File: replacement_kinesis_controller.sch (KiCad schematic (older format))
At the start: 23 parts

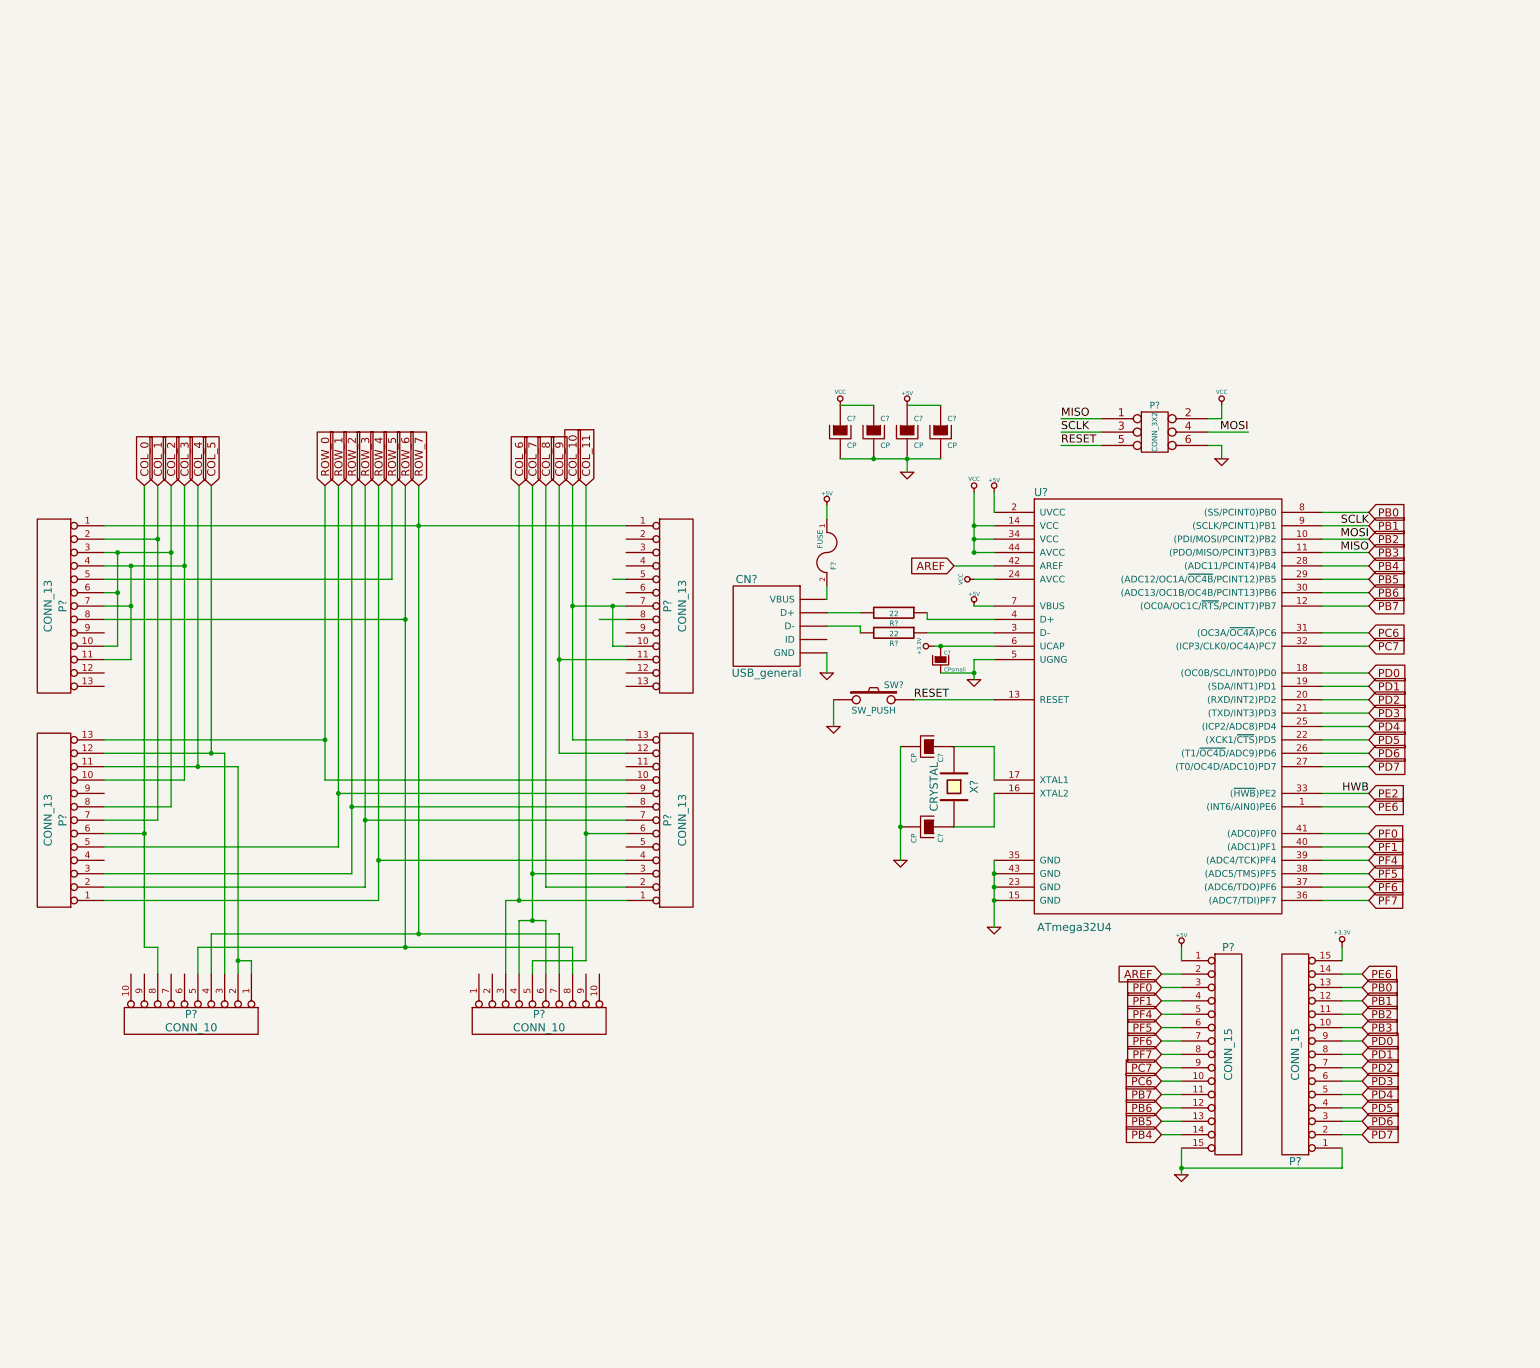
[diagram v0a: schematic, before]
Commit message: Updated schematic with matrix info
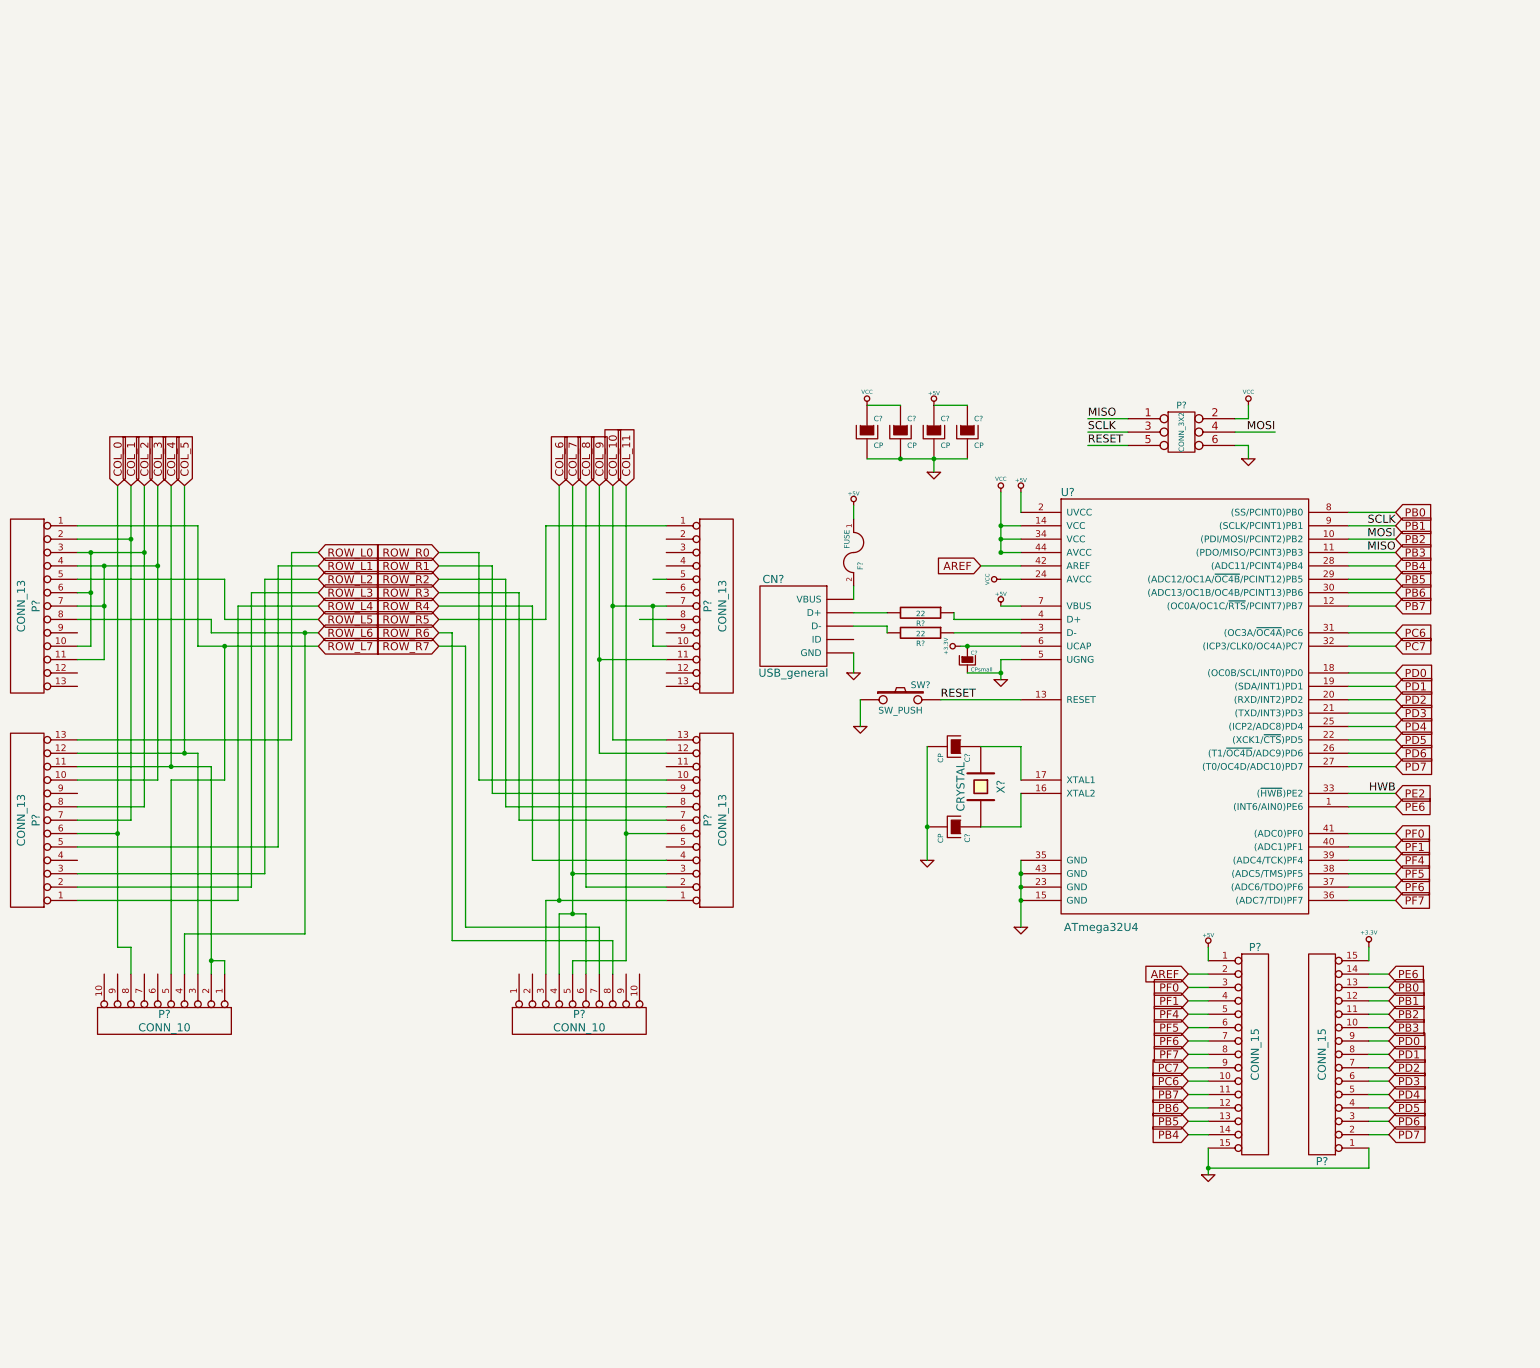
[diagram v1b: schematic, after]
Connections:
- net ROW_0 renamed ROW_L0
- net ROW_L0: no longer P?.10 (P10)
- net ROW_1 renamed ROW_L1
- net ROW_L1: no longer P?.9 (P9)
- net ROW_2 renamed ROW_L2
- net ROW_L2: no longer P?.8 (P8)
- net ROW_3 renamed ROW_L3
- net ROW_L3: no longer P?.7 (P7)
- net ROW_4 renamed ROW_L4
- net ROW_L4: no longer P?.4 (P4)
- net ROW_5 renamed ROW_L5
- removed net ROW_6: P?.5 (P5), P?.8 (P8), P?.8 (P8)
- removed net ROW_7: P?.1 (P1), P?.1 (P1), P?.4 (P4), P?.7 (P7)
- new net ROW_L6: P?.4 (P4), P?.8 (P8)
- new net ROW_L7: P?.1 (P1), P?.5 (P5)
- new net ROW_R0: P?.10 (P10)
- new net ROW_R1: P?.9 (P9)
- new net ROW_R2: P?.8 (P8)
- new net ROW_R3: P?.7 (P7)
- new net ROW_R4: P?.4 (P4)
- new net ROW_R5: P?.1 (P1)
- new net ROW_R6: P?.8 (P8)
- new net ROW_R7: P?.7 (P7)
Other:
- moved on the sheet: C?, CN?, F?, P?, R?, SW?, U?, X?

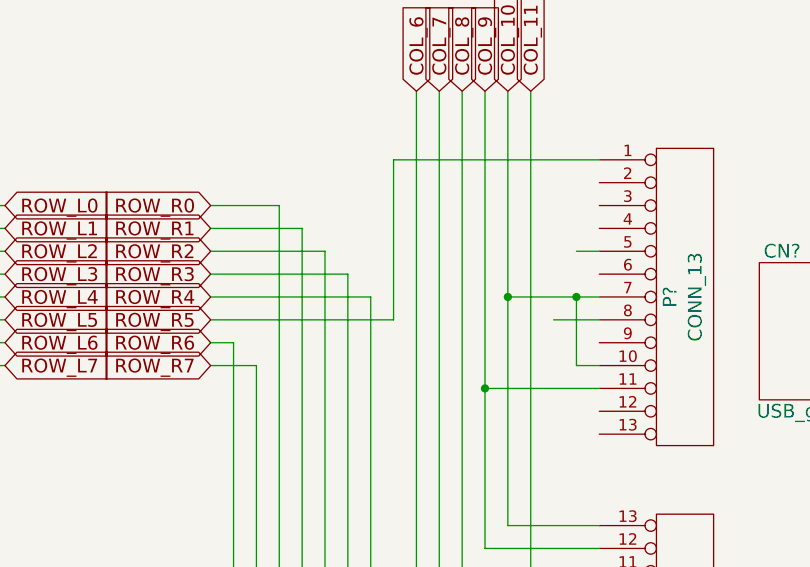
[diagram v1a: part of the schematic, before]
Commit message: Fix up right function key matrix
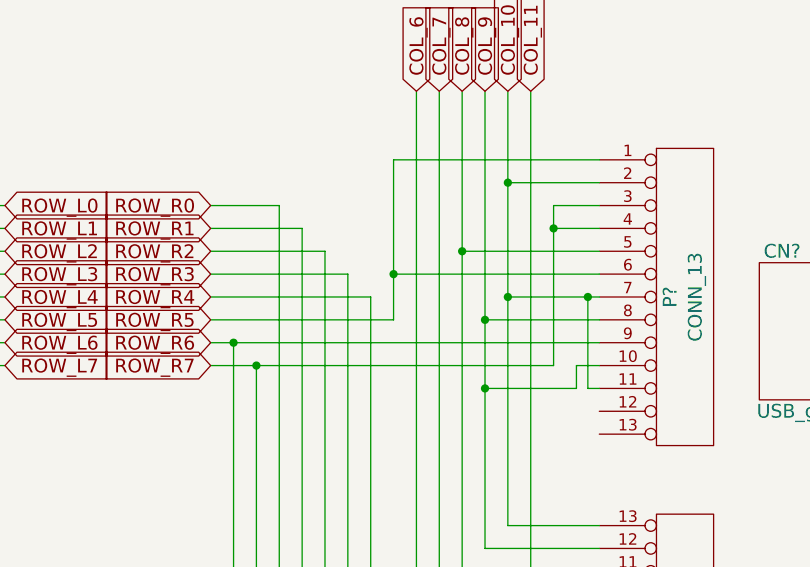
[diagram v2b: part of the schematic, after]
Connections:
- net COL_10: now also P?.11 (P11), P?.2 (P2); no longer P?.10 (P10)
- net COL_8: now also P?.5 (P5)
- net COL_9: now also P?.10 (P10), P?.8 (P8); no longer P?.11 (P11)
- net ROW_R5: now also P?.6 (P6)
- net ROW_R6: now also P?.9 (P9)
- net ROW_R7: now also P?.3 (P3), P?.4 (P4)
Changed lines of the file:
@@
 Connection ~ 1200 2200
 Wire Wire Line
-	5400 2000 5300 2000
-Wire Wire Line
 	5400 2200 5000 2200
 Wire Wire Line
 	5000 1300 5000 3200
-Wire Wire Line
-	5200 2300 5400 2300
-Wire Wire Line
-	5400 2500 5300 2500
-Wire Wire Line
-	5300 2500 5300 2200
-Connection ~ 5300 2200
-Wire Wire Line
-	5400 2600 4900 2600
 Wire Wire Line
 	4900 1300 4900 3300
@@
 	4000 1800 3700 1800
 Wire Wire Line
-	3700 2500 3900 2500
+	3700 2500 5200 2500
 Wire Wire Line
 	4700 1300 4700 4500
@@
 	3800 4700 3800 2400
 Wire Wire Line
-	3800 2400 3700 2400
+	3700 2400 5400 2400
+Wire Wire Line
+	5400 1700 5000 1700
+Connection ~ 5000 1700
+Wire Wire Line
+	5400 1800 5200 1800
+Wire Wire Line
+	5200 1800 5200 2500
+Connection ~ 3900 2500
+Wire Wire Line
+	5400 1900 5200 1900
+Connection ~ 5200 1900
+Wire Wire Line
+	5400 2000 4800 2000
+Connection ~ 4800 2000
+Wire Wire Line
+	5400 2100 4500 2100
+Connection ~ 4500 2100
+Wire Wire Line
+	5400 2300 4900 2300
+Connection ~ 4900 2300
+Connection ~ 3800 2400
+Wire Wire Line
+	5400 2500 5300 2500
+Wire Wire Line
+	5300 2500 5300 2600
+Wire Wire Line
+	5300 2600 4900 2600
+Wire Wire Line
+	5400 2600 5350 2600
+Wire Wire Line
+	5350 2600 5350 2200
+Connection ~ 5350 2200
 $EndSCHEMATC

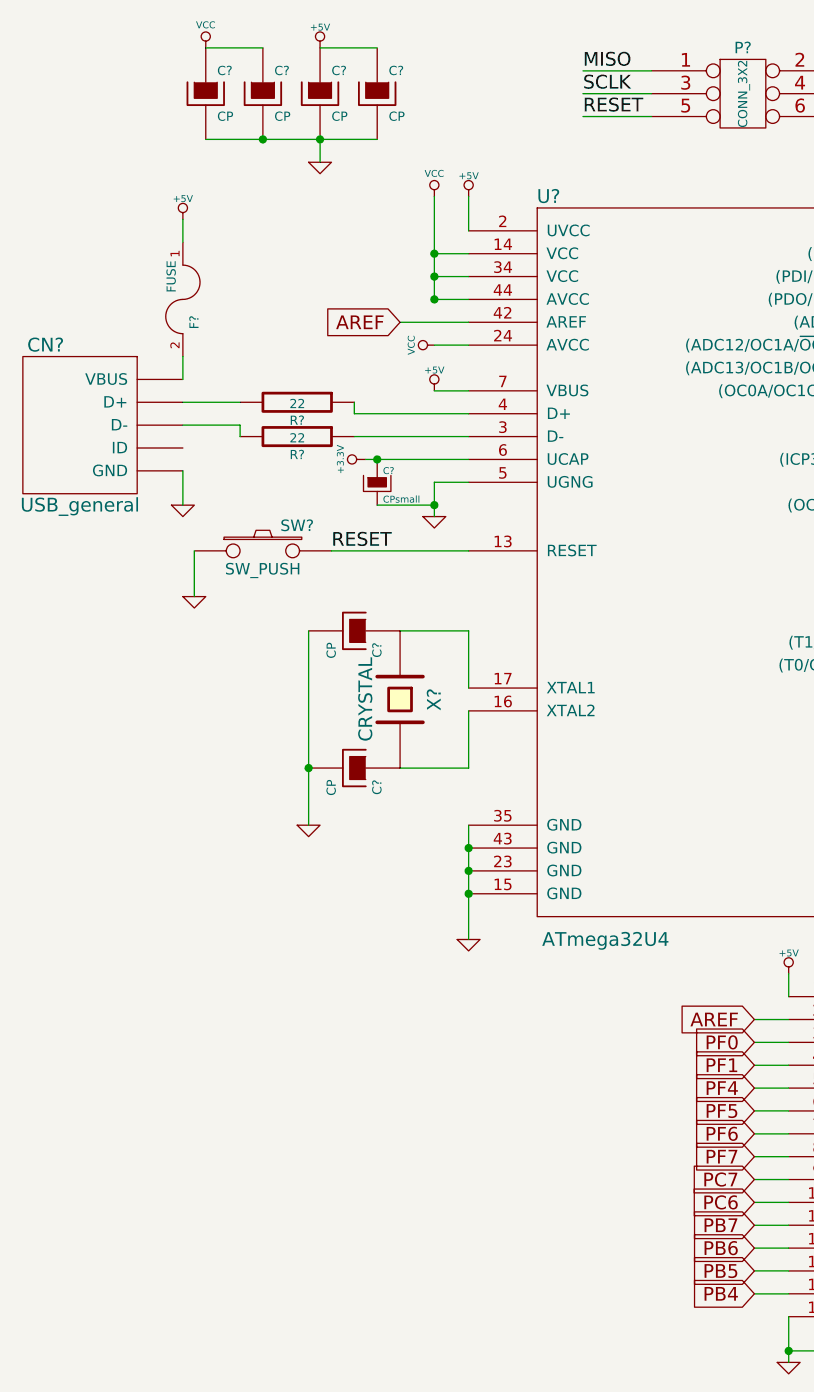
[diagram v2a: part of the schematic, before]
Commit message: Add value and extras for 32u4 breakout schematic
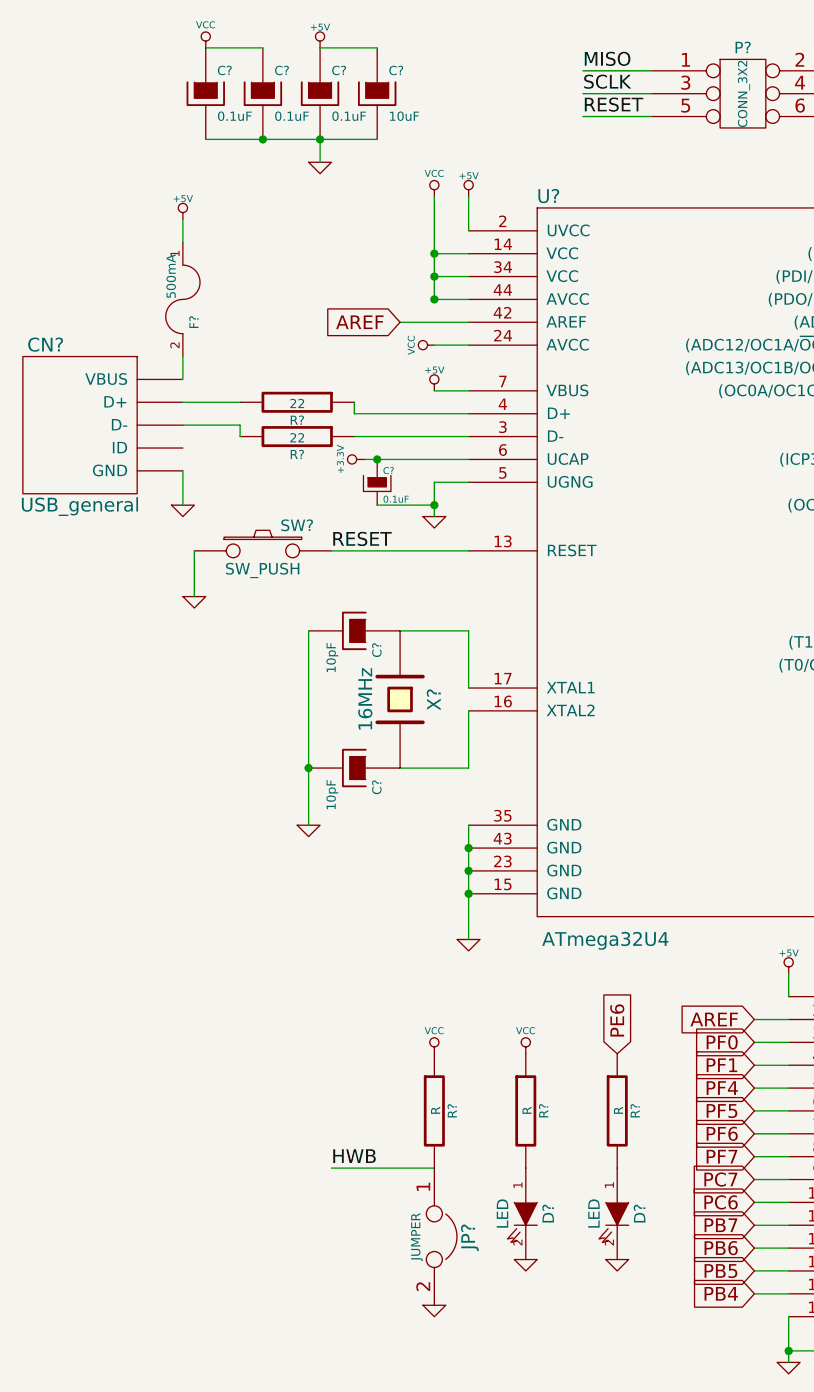
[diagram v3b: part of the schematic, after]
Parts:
- added D? (x2): LED, symbol LED
- added JP?: JUMPER, symbol JUMPER
- added R? (x3): R, symbol R
- C? (x2): value CP -> 10pF
- C?: value CPsmall -> 0.1uF
- C? (x3): value CP -> 0.1uF
- C?: value CP -> 10uF
- F?: value FUSE -> 500mA
- X?: value CRYSTAL -> 16MHz
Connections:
- net GND: now also D?.2 (K), D?.2 (K), JP?.2
- net PE2: now also JP?.1, R?.2
- net PE6: now also R?.1
- net VCC: now also R?.1, R?.1
- new net: D?.1 (A), R?.2 (x2)
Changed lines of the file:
@@
 P 7750 3550
 F 0 "X?" H 7750 3700 60  0000 C CNN
-F 1 "CRYSTAL" H 7750 3400 60  0000 C CNN
+F 1 "16MHz" H 7750 3400 60  0000 C CNN
 F 2 "" H 7750 3550 60  0000 C CNN
 F 3 "" H 7750 3550 60  0000 C CNN
@@
 P 7550 3850
 F 0 "C?" H 7600 3950 40  0000 L CNN
-F 1 "CP" H 7600 3750 40  0000 L CNN
+F 1 "10pF" H 7600 3750 40  0000 L CNN
 F 2 "" H 7650 3700 30  0000 C CNN
 F 3 "" H 7550 3850 300 0000 C CNN
@@
 P 7550 3250
 F 0 "C?" H 7600 3350 40  0000 L CNN
-F 1 "CP" H 7600 3150 40  0000 L CNN
+F 1 "10pF" H 7600 3150 40  0000 L CNN
 F 2 "" H 7650 3100 30  0000 C CNN
 F 3 "" H 7550 3250 300 0000 C CNN
@@
 P 6800 1800
 F 0 "F?" H 6900 1850 40  0000 C CNN
-F 1 "FUSE" H 6700 1750 40  0000 C CNN
+F 1 "500mA" H 6700 1750 40  0000 C CNN
 F 2 "" H 6800 1800 60  0000 C CNN
 F 3 "" H 6800 1800 60  0000 C CNN
@@
 P 7650 2600
 F 0 "C?" H 7675 2650 30  0000 L CNN
-F 1 "CPsmall" H 7675 2525 30  0000 L CNN
+F 1 "0.1uF" H 7675 2525 30  0000 L CNN
 F 2 "" H 7650 2600 60  0000 C CNN
 F 3 "" H 7650 2600 60  0000 C CNN
@@
 P 6900 900
 F 0 "C?" H 6950 1000 40  0000 L CNN
-F 1 "CP" H 6950 800 40  0000 L CNN
+F 1 "0.1uF" H 6950 800 40  0000 L CNN
 F 2 "" H 7000 750 30  0000 C CNN
 F 3 "" H 6900 900 300 0000 C CNN
@@
 P 7150 900
 F 0 "C?" H 7200 1000 40  0000 L CNN
-F 1 "CP" H 7200 800 40  0000 L CNN
+F 1 "0.1uF" H 7200 800 40  0000 L CNN
 F 2 "" H 7250 750 30  0000 C CNN
 F 3 "" H 7150 900 300 0000 C CNN
@@
 P 7400 900
 F 0 "C?" H 7450 1000 40  0000 L CNN
-F 1 "CP" H 7450 800 40  0000 L CNN
+F 1 "0.1uF" H 7450 800 40  0000 L CNN
 F 2 "" H 7500 750 30  0000 C CNN
 F 3 "" H 7400 900 300 0000 C CNN
@@
 P 7650 900
 F 0 "C?" H 7700 1000 40  0000 L CNN
-F 1 "CP" H 7700 800 40  0000 L CNN
+F 1 "10uF" H 7700 800 40  0000 L CNN
 F 2 "" H 7750 750 30  0000 C CNN
 F 3 "" H 7650 900 300 0000 C CNN
@@
 	5350 2600 5350 2200
 Connection ~ 5350 2200
+$Comp
+L R R?
+U 1 1 54C9D2DF
+P 7900 5350
+F 0 "R?" V 7980 5350 40  0000 C CNN
+F 1 "R" V 7907 5351 40  0000 C CNN
+F 2 "" V 7830 5350 30  0000 C CNN
+F 3 "" H 7900 5350 30  0000 C CNN
+	1    7900 5350
+	1    0    0    -1
+$EndComp
+$Comp
+L R R?
+U 1 1 54C9D340
+P 8700 5350
+F 0 "R?" V 8780 5350 40  0000 C CNN
+F 1 "R" V 8707 5351 40  0000 C CNN
+F 2 "" V 8630 5350 30  0000 C CNN
+F 3 "" H 8700 5350 30  0000 C CNN
+	1    8700 5350
+	1    0    0    -1
+$EndComp
+$Comp
+L R R?
+U 1 1 54C9D377
+P 8300 5350
+F 0 "R?" V 8380 5350 40  0000 C CNN
+F 1 "R" V 8307 5351 40  0000 C CNN
+F 2 "" V 8230 5350 30  0000 C CNN
+F 3 "" H 8300 5350 30  0000 C CNN
+	1    8300 5350
+	1    0    0    -1
+$EndComp
+$Comp
+L LED D?
+U 1 1 54C9D45A
+P 8300 5800
+F 0 "D?" H 8300 5900 50  0000 C CNN
+F 1 "LED" H 8300 5700 50  0000 C CNN
+F 2 "" H 8300 5800 60  0000 C CNN
+F 3 "" H 8300 5800 60  0000 C CNN
+	1    8300 5800
+	0    1    1    0
+$EndComp
+$Comp
+L LED D?
+U 1 1 54C9D4B9
+P 8700 5800
+F 0 "D?" H 8700 5900 50  0000 C CNN
+F 1 "LED" H 8700 5700 50  0000 C CNN
+F 2 "" H 8700 5800 60  0000 C CNN
+F 3 "" H 8700 5800 60  0000 C CNN
+	1    8700 5800
+	0    1    1    0
+$EndComp
+$Comp
+L JUMPER JP?
+U 1 1 54C9D61C
+P 7900 5900
+F 0 "JP?" H 7900 6050 60  0000 C CNN
+F 1 "JUMPER" H 7900 5820 40  0000 C CNN
+F 2 "" H 7900 5900 60  0000 C CNN
+F 3 "" H 7900 5900 60  0000 C CNN
+	1    7900 5900
+	0    1    1    0
+$EndComp
+$Comp
+L VCC #PWR?
+U 1 1 54C9D8DB
+P 8300 5100
+F 0 "#PWR?" H 8300 5200 30  0001 C CNN
+F 1 "VCC" H 8300 5200 30  0000 C CNN
+F 2 "" H 8300 5100 60  0000 C CNN
+F 3 "" H 8300 5100 60  0000 C CNN
+	1    8300 5100
+	1    0    0    -1
+$EndComp
+$Comp
+L VCC #PWR?
+U 1 1 54C9D977
+P 7900 5100
+F 0 "#PWR?" H 7900 5200 30  0001 C CNN
+F 1 "VCC" H 7900 5200 30  0000 C CNN
+F 2 "" H 7900 5100 60  0000 C CNN
+F 3 "" H 7900 5100 60  0000 C CNN
+	1    7900 5100
+	1    0    0    -1
+$EndComp
+$Comp
+L GND #PWR?
+U 1 1 54C9D99F
+P 8300 6000
+F 0 "#PWR?" H 8300 6000 30  0001 C CNN
+F 1 "GND" H 8300 5930 30  0001 C CNN
+F 2 "" H 8300 6000 60  0000 C CNN
+F 3 "" H 8300 6000 60  0000 C CNN
+	1    8300 6000
+	1    0    0    -1
+$EndComp
+$Comp
+L GND #PWR?
+U 1 1 54C9D9C7
+P 7900 6200
+F 0 "#PWR?" H 7900 6200 30  0001 C CNN
+F 1 "GND" H 7900 6130 30  0001 C CNN
+F 2 "" H 7900 6200 60  0000 C CNN
+F 3 "" H 7900 6200 60  0000 C CNN
+	1    7900 6200
+	1    0    0    -1
+$EndComp
+$Comp
+L GND #PWR?
+U 1 1 54C9D9EF
+P 8700 6000
+F 0 "#PWR?" H 8700 6000 30  0001 C CNN
+F 1 "GND" H 8700 5930 30  0001 C CNN
+F 2 "" H 8700 6000 60  0000 C CNN
+F 3 "" H 8700 6000 60  0000 C CNN
+	1    8700 6000
+	1    0    0    -1
+$EndComp
+Text GLabel 8700 5100 1    60   Input ~ 0
+PE6
+Wire Wire Line
+	7900 5600 7450 5600
+Text Label 7450 5600 0    60   ~ 0
+HWB
 $EndSCHEMATC
